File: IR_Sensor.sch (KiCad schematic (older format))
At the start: 27 parts, among them Q1 AO3401, Q3 NJL7302L-F3, U12 AE-BME280, U17 OSRB38C9AA, U26 CM1293A-04SO

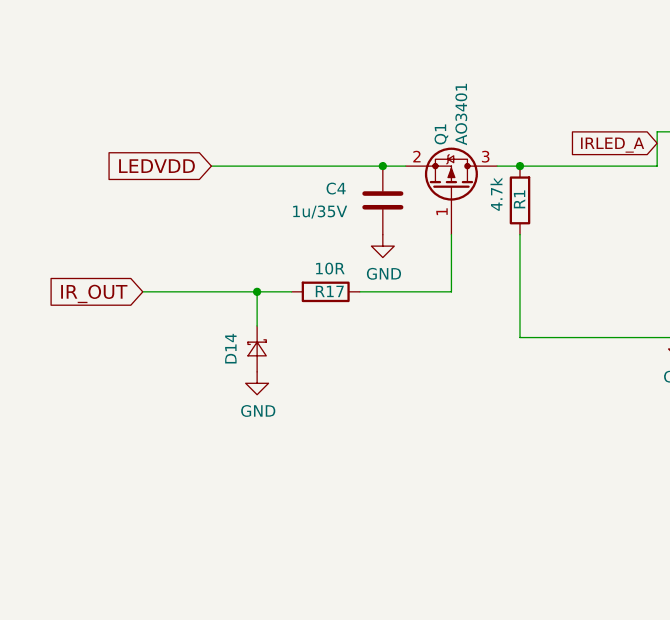
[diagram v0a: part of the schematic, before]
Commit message: Added external IR remote-controller connector; DRC clear
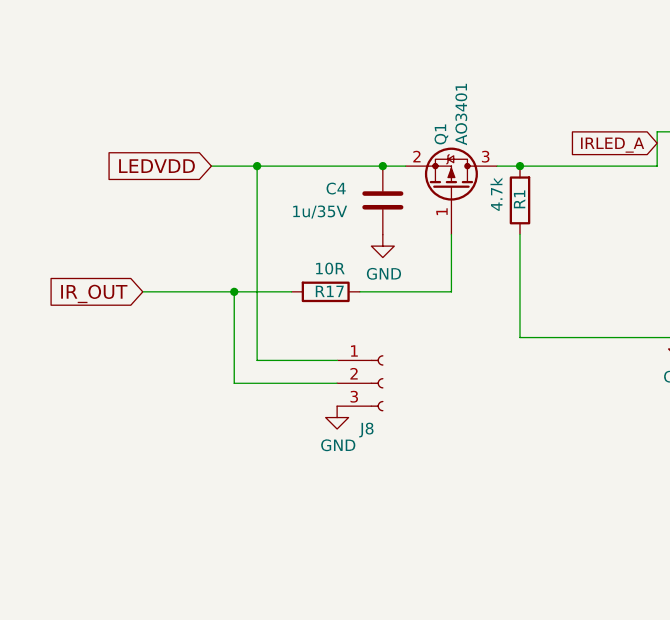
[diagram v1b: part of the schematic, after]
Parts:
- removed D14: D_Schottky_Small, components:SOD-523-mod, symbol dotmatrix_64x48-rescue:D_Schottky_Small-device
- added J8: Conn_01x03_Female, Connector_PinHeader_2.54mm:PinHeader_1x03_P2.54mm_Vertical, symbol dotmatrix_64x48-rescue:Conn_01x03_Female-Connector
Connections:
- wire segments 97 -> 101
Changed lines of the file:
@@
 Text GLabel 1050 3300 0    60   Input ~ 0
 IR_OUT
-$Comp
-L dotmatrix_64x48-rescue:D_Schottky_Small-device D14
-U 1 1 59A7F6B4
-P 1550 3550
-F 0 "D14" H 1550 3437 50  0000 C CNN
-F 1 "D_Schottky_Small" H 1550 3436 50  0001 C CNN
-F 2 "components:SOD-523-mod" H 1550 3436 50  0001 C CNN
-F 3 "" V 1550 3550 50  0000 C CNN
-	1    1550 3550
-	0    1    1    0
-$EndComp
-$Comp
-L dotmatrix_64x48-rescue:GND-power #PWR038
-U 1 1 59A7F6BB
-P 1550 3650
-F 0 "#PWR038" H 1550 3400 50  0001 C CNN
-F 1 "GND" H 1555 3477 50  0000 C CNN
-F 2 "" H 1550 3650 50  0000 C CNN
-F 3 "" H 1550 3650 50  0000 C CNN
-	1    1550 3650
-	1    0    0    -1
-$EndComp
-Wire Wire Line
-	1550 3450 1550 3300
-Wire Wire Line
-	1050 3300 1550 3300
-Connection ~ 1550 3300
 Wire Wire Line
 	1350 1550 1750 1550
@@
 Wire Wire Line
 	4600 1800 4900 1800
-Wire Wire Line
-	1550 3300 1700 3300
 $Comp
 L dotmatrix_64x48-rescue:LED-device LED49
@@
 LED1642VDD
 Wire Wire Line
-	1350 2750 2100 2750
+	1350 2750 1550 2750
+Wire Wire Line
+	1050 3300 1450 3300
+$Comp
+L dotmatrix_64x48-rescue:Conn_01x03_Female-Connector J8
+U 1 1 5DD670C3
+P 2100 3700
+F 0 "J8" H 2000 3500 50  0000 L CNN
+F 1 "Conn_01x03_Female" H 1500 3950 50  0001 L CNN
+F 2 "Connector_PinHeader_2.54mm:PinHeader_1x03_P2.54mm_Vertical" H 2100 3700 50  0001 C CNN
+F 3 "" H 2100 3700 50  0001 C CNN
+	1    2100 3700
+	1    0    0    -1
+$EndComp
+Wire Wire Line
+	1550 2750 1550 3600
+Wire Wire Line
+	1550 3600 1900 3600
+Connection ~ 1550 2750
+Wire Wire Line
+	1550 2750 2100 2750
+Wire Wire Line
+	1450 3300 1450 3700
+Wire Wire Line
+	1450 3700 1900 3700
+Connection ~ 1450 3300
+Wire Wire Line
+	1450 3300 1700 3300
+$Comp
+L dotmatrix_64x48-rescue:GND-power #PWR0138
+U 1 1 5DD66DE4
+P 1900 3800
+F 0 "#PWR0138" H 1900 3550 50  0001 C CNN
+F 1 "GND" H 1905 3627 50  0000 C CNN
+F 2 "" H 1900 3800 50  0000 C CNN
+F 3 "" H 1900 3800 50  0000 C CNN
+	1    1900 3800
+	1    0    0    -1
+$EndComp
 $EndSCHEMATC

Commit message: Fixed USB micro-b's mount polarity; Improved SOT-23-6 1-pin silk marker readability
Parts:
- U26: footprint TO_SOT_Packages_SMD:SOT-23-6_Handsoldering -> components:SOT-23-6_Handsoldering_mod
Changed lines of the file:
@@
 F 0 "U26" H 9400 6328 50  0000 C CNN
 F 1 "CM1293A-04SO" H 9400 6237 50  0000 C CNN
-F 2 "TO_SOT_Packages_SMD:SOT-23-6_Handsoldering" H 9400 5650 50  0001 C CNN
+F 2 "components:SOT-23-6_Handsoldering_mod" H 9400 5650 50  0001 C CNN
 F 3 "http://www.onsemi.com/pub/Collateral/SRV05-4-D.PDF" H 9400 5650 50  0001 C CNN
 	1    9400 5650

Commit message: Changed I2S ESD diode's returning VDD from LED1642VDD to LEDLOGICVDD
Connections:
- net labels removed: LED1642VDD
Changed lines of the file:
@@
 	7750 1650 7750 1500
 Text GLabel 10250 5150 2    60   Input ~ 0
-LED1642VDD
+LEDLOGICVDD
 Wire Wire Line
 	1350 2750 1550 2750

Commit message: Fixed IR LED drive voltage range
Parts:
- added Q31: Q_NPN_BEC, Package_TO_SOT_SMD:SOT-23_Handsoldering, symbol dotmatrix_64x48-rescue:Q_NPN_BEC-device
- added R79: 1k, Resistor_SMD:R_0603_1608Metric_Pad1.05x0.95mm_HandSolder, symbol dotmatrix_64x48-rescue:R-device
- added R80: 10k, Resistor_SMD:R_0603_1608Metric_Pad1.05x0.95mm_HandSolder, symbol dotmatrix_64x48-rescue:R-device
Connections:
- wire segments 101 -> 104
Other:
- moved on the sheet: C4, LED49, Q1, R1, R139, R140, R16, R17, R26
